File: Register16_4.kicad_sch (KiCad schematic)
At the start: 4 parts

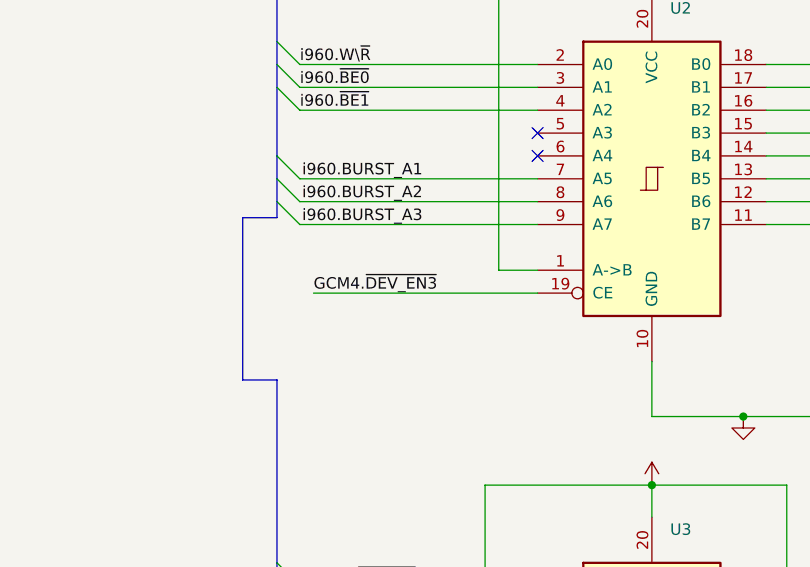
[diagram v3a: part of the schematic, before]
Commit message: Use a third 4809 running independently to act as glue and startup unit.
I was able to remove a nor gate ic by adding. I am also planning to use
the CCLs for other features as well. Perhaps as a simpler inverter.
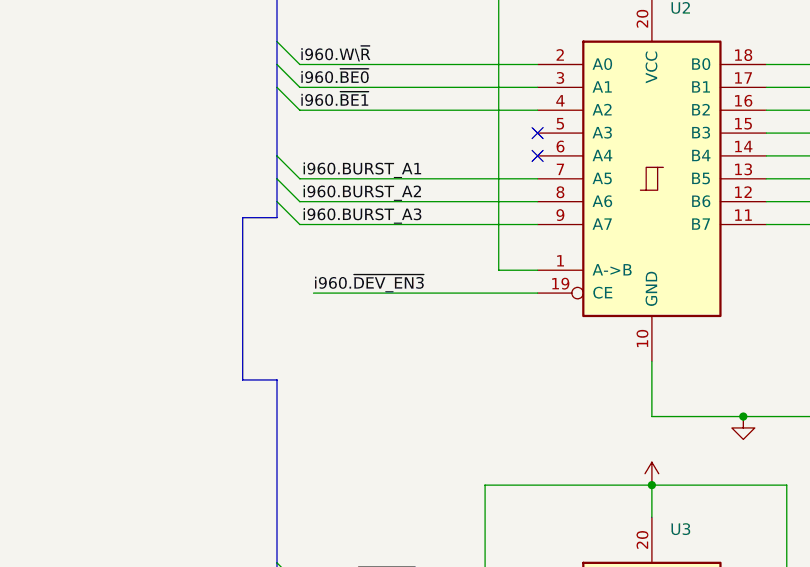
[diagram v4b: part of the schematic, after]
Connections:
- net GCM4.~{DEV_EN3}: no longer U2.19 (CE)
- new net i960.~{DEV_EN3}: U2.19 (CE)
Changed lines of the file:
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@@
     (effects (font (size 1.27 1.27)) (justify right bottom))
   )
-  (label "GCM4.~{DEV_EN3}" (at 104.648 65.532 0)
+  (label "i960.~{DEV_EN3}" (at 104.648 65.532 0)
     (effects (font (size 1.27 1.27)) (justify left bottom))
   )

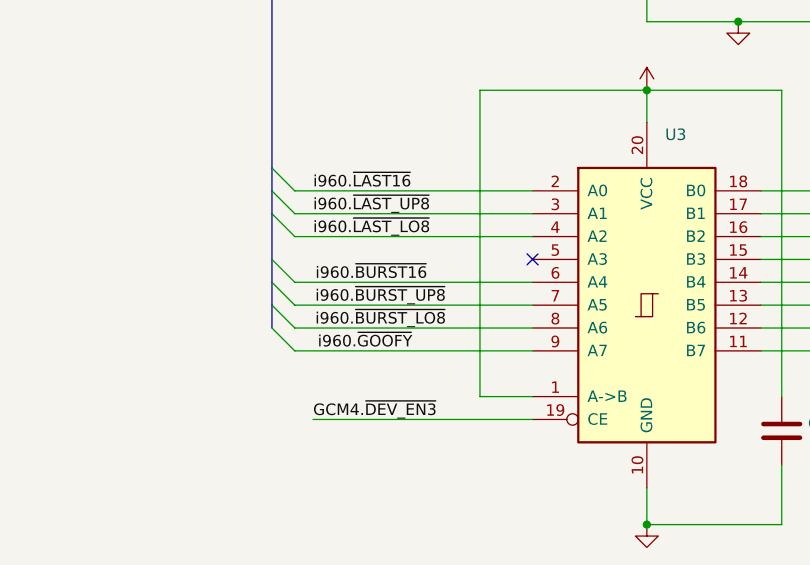
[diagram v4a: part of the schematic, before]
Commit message: Added a communication channel between the different glue chips.
I am considering connecting this up to the chipset through glue
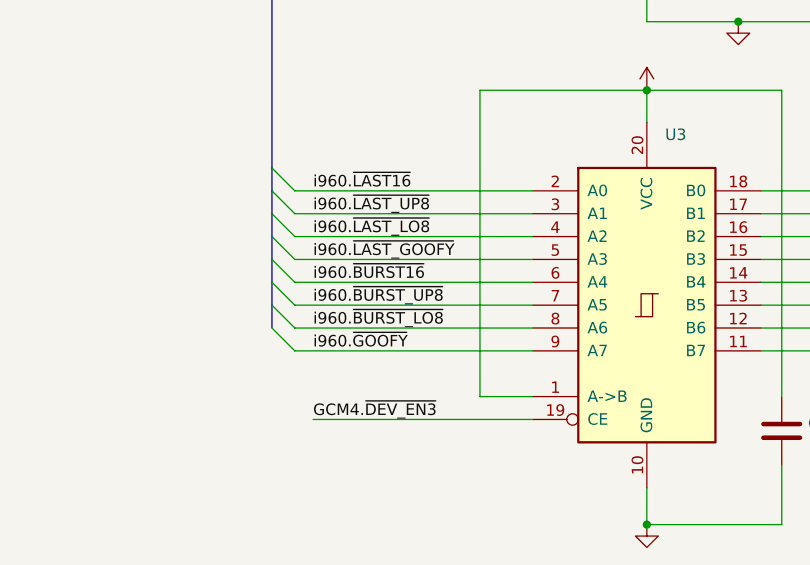
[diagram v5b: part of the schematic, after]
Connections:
- net i960.~{LAST_GOOFY}: now reaches U3.5 (A3)
- no-connect marks 3 -> 2
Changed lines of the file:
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@@
   (no_connect (at 129.54 47.752))
   (no_connect (at 129.54 50.292))
-  (no_connect (at 129.54 105.664))
   (bus_entry (at 100.584 113.284) (size 2.54 2.54)
     (stroke (width 0) (type default) (color 0 0 0 0))
@@
     (stroke (width 0) (type default) (color 0 0 0 0))
   )
+  (bus_entry (at 100.584 103.124) (size 2.54 2.54)
+    (stroke (width 0) (type default) (color 0 0 0 0))
+  )
   (bus_entry (at 100.584 42.672) (size 2.54 2.54)
     (stroke (width 0) (type default) (color 0 0 0 0))
@@
     (stroke (width 0) (type default) (color 0 0 0 0))
   )
-  (bus (pts (xy 100.584 100.584) (xy 100.584 105.664))
+  (bus (pts (xy 100.584 100.584) (xy 100.584 103.124))
     (stroke (width 0) (type default) (color 0 0 0 0))
   )
@@
     (stroke (width 0) (type default) (color 0 0 0 0))
   )
+  (wire (pts (xy 103.124 105.664) (xy 129.54 105.664))
+    (stroke (width 0) (type default) (color 0 0 0 0))
+  )
   (bus (pts (xy 100.584 75.184) (xy 96.774 75.184))
     (stroke (width 0) (type default) (color 0 0 0 0))
@@
     (stroke (width 0) (type default) (color 0 0 0 0))
   )
+  (bus (pts (xy 100.584 103.124) (xy 100.584 105.664))
+    (stroke (width 0) (type default) (color 0 0 0 0))
+  )
   (bus (pts (xy 100.584 98.044) (xy 100.584 95.504))
     (stroke (width 0) (type default) (color 0 0 0 0))
@@
     (effects (font (size 1.27 1.27)) (justify left bottom))
   )
-  (label "i960.~{GOOFY}" (at 105.664 115.824 0)
-    (effects (font (size 1.27 1.27)) (justify left bottom))
-  )
-  (label "i960.~{BURST16}" (at 105.41 108.204 0)
+  (label "i960.~{GOOFY}" (at 105.156 115.824 0)
+    (effects (font (size 1.27 1.27)) (justify left bottom))
+  )
+  (label "i960.~{BURST16}" (at 105.156 108.204 0)
     (effects (font (size 1.27 1.27)) (justify left bottom))
   )
@@
     (effects (font (size 1.27 1.27)) (justify left bottom))
   )
-  (label "i960.~{BURST_UP8}" (at 105.3927 110.744 0)
+  (label "i960.~{BURST_UP8}" (at 105.156 110.744 0)
     (effects (font (size 1.27 1.27)) (justify left bottom))
   )
@@
     (effects (font (size 1.27 1.27)) (justify right bottom))
   )
+  (label "i960.~{LAST_GOOFY}" (at 105.156 105.664 0)
+    (effects (font (size 1.27 1.27)) (justify left bottom))
+  )
   (label "i960.W\\~{R}" (at 103.124 40.132 0)
     (effects (font (size 1.27 1.27)) (justify left bottom))
   )
-  (label "i960.~{BURST_LO8}" (at 105.3927 113.284 0)
-    (effects (font (size 1.27 1.27)) (justify left bottom))
-  )
+  (label "i960.~{BURST_LO8}" (at 105.156 113.284 0)
+    (effects (font (size 1.27 1.27)) (justify left bottom))
+  )
